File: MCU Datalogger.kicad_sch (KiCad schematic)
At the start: 25 parts, among them U1 ATMEGA328P-AU, U2 DS1337S_, U3 24LC1025, U4 24LC1025, Y1 32.768 KHz, Y2 16MHz

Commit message: Footprints Fixed
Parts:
- BT1: footprint (none) -> Connector_PinHeader_2.54mm:PinHeader_2x01_P2.54mm_Vertical
- C1, C2, C3, C4, C5: footprint (none) -> Capacitor_SMD:C_0805_2012Metric
- D1, D2: footprint (none) -> LED_SMD:LED_0805_2012Metric
- H1, H2, H3, H4: footprint (none) -> MountingHole:MountingHole_2.1mm
- R1, R2, R3, R4, R5, R6, R7: footprint (none) -> Resistor_SMD:R_0805_2012Metric
- U1: renamed from U3; footprint (none) -> Package_SO:SOIC-8_5.3x5.3mm_P1.27mm
- U2: footprint DS1337S_:SOIC127P600X175-8N -> Package_SO:SOIC-8_5.3x5.3mm_P1.27mm
- U3: renamed from U4; footprint (none) -> Package_SO:SOIC-8_5.3x5.3mm_P1.27mm
- U4: renamed from U1; footprint ATMEGA328P-AU:QFP80P900X900X120-32N -> FOOTPRINTS:ATMEGA
- Y1, Y2: footprint (none) -> Crystal:Crystal_SMD_5032-2Pin_5.0x3.2mm_HandSoldering
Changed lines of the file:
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@@
 		(on_board yes)
 		(dnp no)
-		(property "Reference" "U4"
+		(property "Reference" "U3"
 			(at 80.518 133.35 0)
 			(effects
@@
 		(property "Value" "24LC1025"
 			(at 80.518 135.89 0)
-			(effects
-				(font
-					(size 1.27 1.27)
-				)
-				(justify left)
-			)
-		)
-		(property "Footprint" ""
+			(show_name yes)
+			(effects
+				(font
+					(size 1.27 1.27)
+				)
+				(justify left)
+			)
+		)
+		(property "Footprint" "Package_SO:SOIC-8_5.3x5.3mm_P1.27mm"
 			(at 91.44 146.05 0)
 			(effects
@@
 			)
 		)
+		(property "Purpose" ""
+			(at 91.44 146.05 0)
+			(effects
+				(font
+					(size 1.27 1.27)
+				)
+			)
+		)
 		(pin "5"
 		)
@@
 			(project ""
 				(path "/932db461-6a18-4fd3-9410-5532f4da7c4e"
-					(reference "U4")
+					(reference "U3")
 					(unit 1)
 				)
@@
 			)
 		)
-		(property "Footprint" ""
+		(property "Footprint" "Capacitor_SMD:C_0805_2012Metric"
 			(at 153.67 58.1152 0)
 			(effects
@@
 			)
 		)
-		(property "Footprint" ""
+		(property "Footprint" "LED_SMD:LED_0805_2012Metric"
 			(at 172.72 46.99 0)
 			(effects
@@
 			)
 		)
-		(property "Footprint" ""
+		(property "Footprint" "Crystal:Crystal_SMD_5032-2Pin_5.0x3.2mm_HandSoldering"
 			(at 175.26 63.5 0)
 			(effects
@@
 			)
 		)
-		(property "Footprint" ""
+		(property "Footprint" "MountingHole:MountingHole_2.1mm"
 			(at 248.92 140.97 0)
 			(effects
@@
 			)
 		)
-		(property "Footprint" ""
+		(property "Footprint" "Resistor_SMD:R_0805_2012Metric"
 			(at 87.122 57.15 90)
 			(effects
@@
 		(on_board yes)
 		(dnp no)
-		(property "Reference" "U3"
+		(property "Reference" "U1"
 			(at 42.164 133.096 0)
 			(effects
@@
 			)
 		)
-		(property "Footprint" ""
+		(property "Footprint" "Package_SO:SOIC-8_5.3x5.3mm_P1.27mm"
 			(at 55.88 146.05 0)
 			(effects
@@
 			)
 		)
+		(property "Purpose" ""
+			(at 55.88 146.05 0)
+			(effects
+				(font
+					(size 1.27 1.27)
+				)
+			)
+		)
 		(pin "3"
 		)
@@
 			(project ""
 				(path "/932db461-6a18-4fd3-9410-5532f4da7c4e"
-					(reference "U3")
+					(reference "U1")
 					(unit 1)
 				)
@@
 			)
 		)
-		(property "Footprint" ""
+		(property "Footprint" "Capacitor_SMD:C_0805_2012Metric"
 			(at 168.91 33.3248 0)
 			(effects
@@
 		(dnp no)
 		(fields_autoplaced yes)
-		(property "Reference" "U1"
+		(property "Reference" "U4"
 			(at 213.36 31.75 0)
 			(effects
@@
 			)
 		)
-		(property "Footprint" "ATMEGA328P-AU:QFP80P900X900X120-32N"
+		(property "Footprint" "FOOTPRINTS:ATMEGA"
 			(at 213.36 64.77 0)
 			(effects
@@
 			)
 		)
+		(property "Purpose" ""
+			(at 213.36 64.77 0)
+			(effects
+				(font
+					(size 1.27 1.27)
+				)
+			)
+		)
 		(pin "15"
 		)
@@
 			(project ""
 				(path "/932db461-6a18-4fd3-9410-5532f4da7c4e"
-					(reference "U1")
+					(reference "U4")
 					(unit 1)
 				)
@@
 			)
 		)
-		(property "Footprint" ""
+		(property "Footprint" "Connector_PinHeader_2.54mm:PinHeader_2x01_P2.54mm_Vertical"
 			(at 267.97 45.466 90)
 			(effects
@@
 			)
 		)
+		(property "Purpose" ""
+			(at 267.97 46.99 0)
+			(effects
+				(font
+					(size 1.27 1.27)
+				)
+			)
+		)
 		(pin "1"
 		)
@@
 			)
 		)
-		(property "Footprint" ""
+		(property "Footprint" "Resistor_SMD:R_0805_2012Metric"
 			(at 157.48 48.768 90)
 			(effects
@@
 			)
 		)
-		(property "Footprint" ""
+		(property "Footprint" "Capacitor_SMD:C_0805_2012Metric"
 			(at 254.9652 49.53 0)
 			(effects
@@
 			)
 		)
-		(property "Footprint" ""
+		(property "Footprint" "Resistor_SMD:R_0805_2012Metric"
 			(at 189.23 86.868 90)
 			(effects
@@
 			)
 		)
-		(property "Footprint" ""
+		(property "Footprint" "Resistor_SMD:R_0805_2012Metric"
 			(at 112.522 146.05 90)
 			(effects
@@
 			)
 		)
-		(property "Footprint" ""
+		(property "Footprint" "Resistor_SMD:R_0805_2012Metric"
 			(at 125.222 146.05 90)
 			(effects
@@
 			)
 		)
-		(property "Footprint" "DS1337S_:SOIC127P600X175-8N"
+		(property "Footprint" "Package_SO:SOIC-8_5.3x5.3mm_P1.27mm"
 			(at 62.23 68.58 0)
 			(effects
@@
 			)
 		)
+		(property "Purpose" ""
+			(at 62.23 68.58 0)
+			(effects
+				(font
+					(size 1.27 1.27)
+				)
+			)
+		)
 		(pin "4"
 		)
@@
 			)
 		)
-		(property "Footprint" ""
+		(property "Footprint" "MountingHole:MountingHole_2.1mm"
 			(at 248.92 149.86 0)
 			(effects
@@
 			)
 		)
-		(property "Footprint" ""
+		(property "Footprint" "Capacitor_SMD:C_0805_2012Metric"
 			(at 153.67 72.0852 0)
 			(effects
@@
 			)
 		)
-		(property "Footprint" ""
+		(property "Footprint" "LED_SMD:LED_0805_2012Metric"
 			(at 247.65 53.34 0)
 			(effects
@@
 			)
 		)
-		(property "Footprint" ""
+		(property "Footprint" "MountingHole:MountingHole_2.1mm"
 			(at 248.92 123.19 0)
 			(effects
@@
 			)
 		)
-		(property "Footprint" ""
+		(property "Footprint" "Crystal:Crystal_SMD_5032-2Pin_5.0x3.2mm_HandSoldering"
 			(at 26.67 68.58 0)
 			(effects
@@
 			)
 		)
-		(property "Footprint" ""
+		(property "Footprint" "Resistor_SMD:R_0805_2012Metric"
 			(at 245.872 67.31 90)
 			(effects
@@
 			)
 		)
-		(property "Footprint" ""
+		(property "Footprint" "Resistor_SMD:R_0805_2012Metric"
 			(at 97.282 57.15 90)
 			(effects
@@
 			)
 		)
-		(property "Footprint" ""
+		(property "Footprint" "Capacitor_SMD:C_0805_2012Metric"
 			(at 111.4552 60.96 0)
 			(effects
@@
 			)
 		)
-		(property "Footprint" ""
+		(property "Footprint" "MountingHole:MountingHole_2.1mm"
 			(at 248.92 132.08 0)
 			(effects

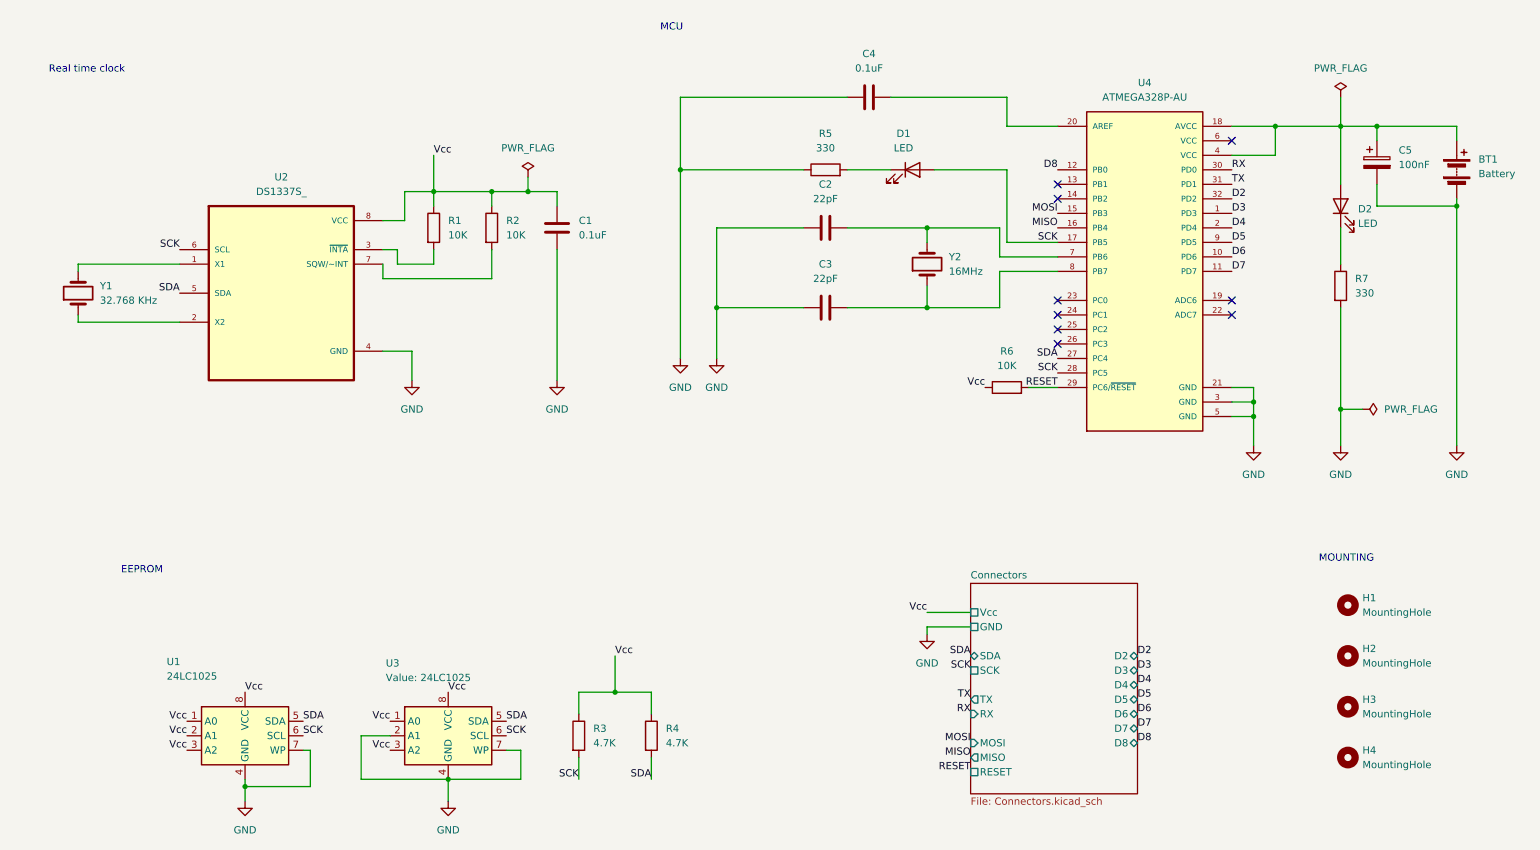
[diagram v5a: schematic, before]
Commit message: Fixed two defects in the schematic.
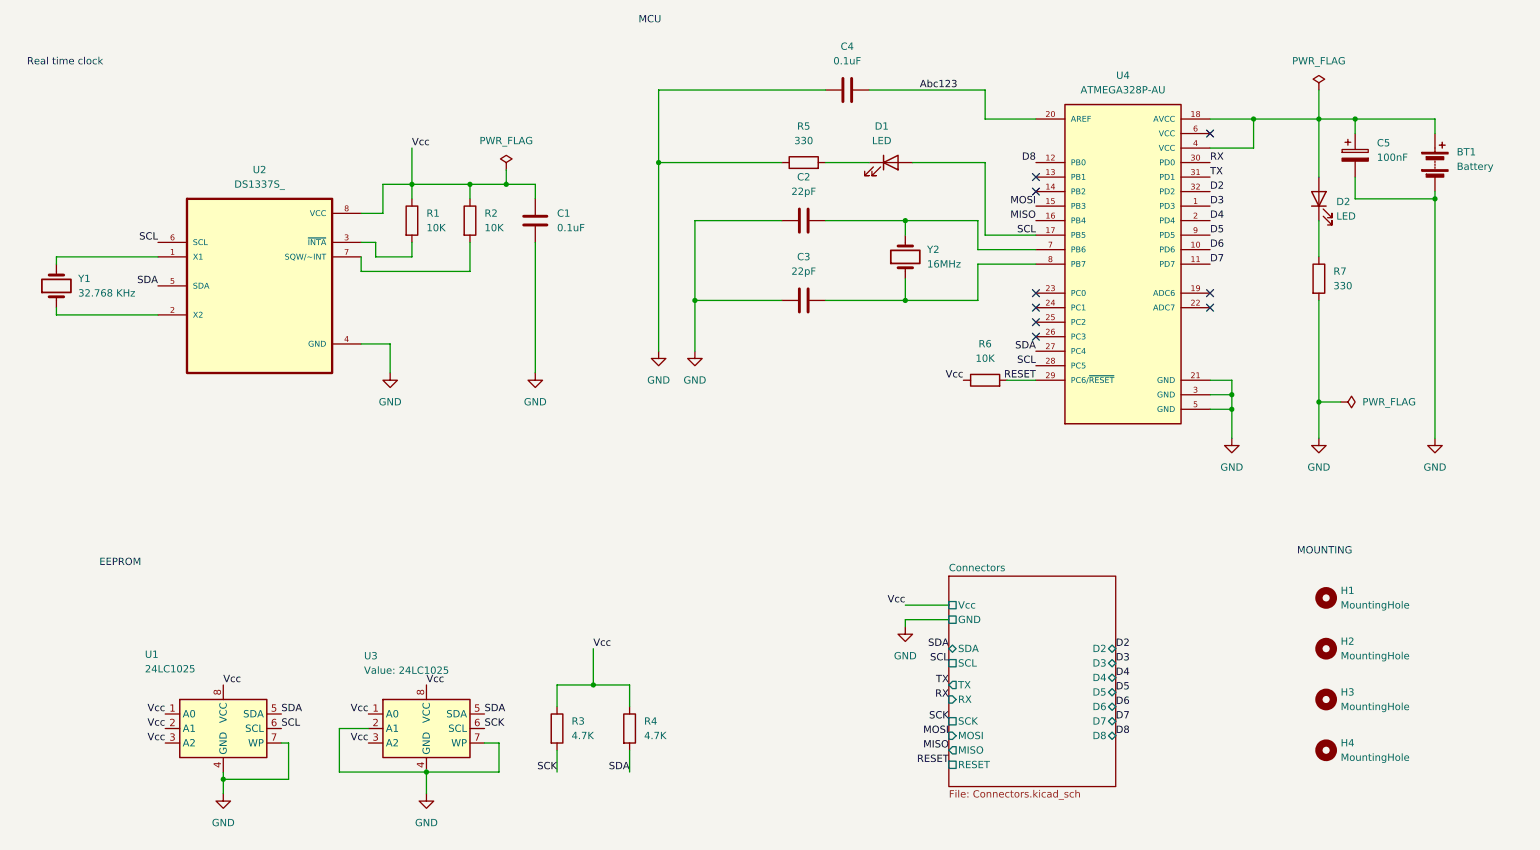
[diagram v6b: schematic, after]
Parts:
- U2: footprint Package_SO:SOIC-8_5.3x5.3mm_P1.27mm -> FOOTPRINTS:DS13375+
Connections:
- net SCK: no longer D1.2 (A), U1.6 (SCL), U2.6 (SCL), U4.17 (PB5), U4.28 (PC5)
- net Abc123: now reaches C4.2, U4.20 (AREF)
- new net SCL: D1.2 (A), U1.6 (SCL), U2.6 (SCL), U4.17 (PB5), U4.28 (PC5)
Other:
- sheet Connectors ports: added SCL; removed none
- title: MCU DATALOGGER WITH MEMORY & CLOCK -> MCU Datalogger with RTC & Memory
- moved on the sheet: BT1, C1, C2, C3, C4, C5, D1, D2, H1, H2, H3, H4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
